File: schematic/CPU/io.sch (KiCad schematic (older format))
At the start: 28 parts, among them SW4 SW_DIP_x08, U72 74LS245, U73 74LS273, U74 ATmega328P-PU, U75 74LS374, U76 DC56-11EWA

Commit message: schematic finished
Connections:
- net labels added: d1a, d1b, d1c, d1d, d1e, d1f, d1g, out0, out1, out2, out3, out4, out5, out6, out7
- wire segments 104 -> 95
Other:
- moved on the sheet: R73, R74, R75, R76, R77, R78, R79, R80, R81, R82, R83, R84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

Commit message: schematic with henry
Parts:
- removed R73, R74, R75, R76, R77, R78, R79, R80, R81, R82, R83, R84, R85, R86, R87, R88, R89, R90, R91, R92, R93, R94: 1k, symbol Device:R
- removed SW4: SW_DIP_x08, symbol Switch:SW_DIP_x08
- removed U72: 74LS245, symbol 74xx:74LS245
- removed U74: ATmega328P-PU, Package_DIP:DIP-28_W7.62mm, symbol MCU_Microchip_ATmega:ATmega328P-PU
- removed U75: 74LS374, symbol 74xx:74LS374
- removed U76: DC56-11EWA, Display_7Segment:DA56-11SURKWA, symbol Display_Character:DC56-11EWA
- added RN10: 10k, Resistor_THT:R_Array_SIP9, symbol Device:R_Network08
- added SW10, SW11: SW_Coded_SH-7050, symbol Switch:SW_Coded_SH-7050
- added U88: 74F521, symbol 8bitCPU-rescue:74F521
- added U89, U90: 74LS32, symbol 74xx:74LS32
- added U91: 74LS245, symbol 74xx:74LS245
- added U93, U94: 5082_7340, symbol 8bitCPU-rescue:5082_7340
- renumbered U73 to U92
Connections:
- net labels added: ioAddr0, ioAddr1, ioAddr2, ioAddr3, ioAddr4, ioAddr5, ioAddr6, ioAddr7, ioSelect, ~ioOE~, ~ioWE~
- net labels removed: d1a, d1b, d1c, d1d, d1e, d1f, d1g, out0, out1, out2, out3, out4, out5, out6, out7, outWRPulse, sr0, sr1, sr2, sr3, sr4, sr5, sr6, ~inOE~
- wire segments 95 -> 113
- no-connect marks 8 -> 0
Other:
- note added: "Invertierung beachten!"
- moved on the sheet: U92

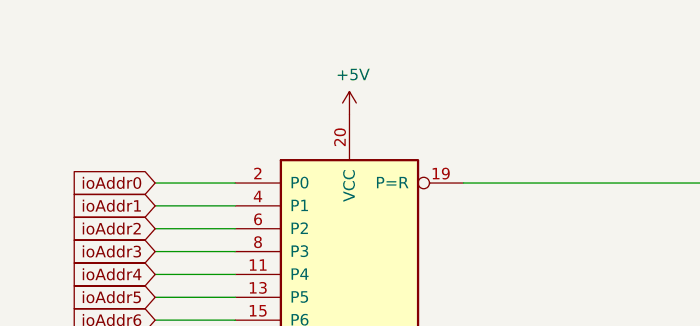
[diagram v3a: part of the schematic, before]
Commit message: updated verilog from schematic
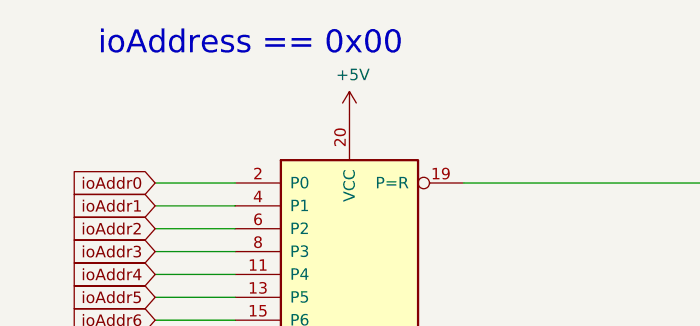
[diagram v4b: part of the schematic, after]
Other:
- note added: "ioAddress == 0x00"
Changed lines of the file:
@@
 Wire Wire Line
 	7000 2450 7550 2450
+Text Notes 1850 1250 0    100  ~ 0
+ioAddress == 0x00
 $EndSCHEMATC

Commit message: renamed project
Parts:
- U88: symbol 8bitCPU-rescue:74F521 -> MEDiC-rescue:74F521
- U93, U94: symbol 8bitCPU-rescue:5082_7340 -> MEDiC-rescue:5082_7340
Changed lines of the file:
@@
 	5700 2450 6000 2450
 $Comp
-L 8bitCPU-rescue:74F521 U88
+L MEDiC-rescue:74F521 U88
 U 1 1 62CAE1E1
 P 3550 2600
@@
 	5800 4350 5950 4350
 $Comp
-L 8bitCPU-rescue:5082_7340 U93
+L MEDiC-rescue:5082_7340 U93
 U 1 1 62D5B960
 P 8850 2250
@@
 	8100 3700 7550 3700
 $Comp
-L 8bitCPU-rescue:5082_7340 U94
+L MEDiC-rescue:5082_7340 U94
 U 1 1 62D6D0EE
 P 8850 3900

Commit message: renamed project
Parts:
- U88: symbol MEDiC-rescue:74F521 -> EDiC-rescue:74F521
- U93, U94: symbol MEDiC-rescue:5082_7340 -> EDiC-rescue:5082_7340
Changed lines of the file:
@@
 	5700 2450 6000 2450
 $Comp
-L MEDiC-rescue:74F521 U88
+L EDiC-rescue:74F521 U88
 U 1 1 62CAE1E1
 P 3550 2600
@@
 	5800 4350 5950 4350
 $Comp
-L MEDiC-rescue:5082_7340 U93
+L EDiC-rescue:5082_7340 U93
 U 1 1 62D5B960
 P 8850 2250
@@
 	8100 3700 7550 3700
 $Comp
-L MEDiC-rescue:5082_7340 U94
+L EDiC-rescue:5082_7340 U94
 U 1 1 62D6D0EE
 P 8850 3900

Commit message: restructured folders
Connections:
- net ioSelect renamed ~ioCE~
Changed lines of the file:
@@
 $EndComp
 Text GLabel 2000 3600 0    50   Input ~ 0
-ioSelect
+~ioCE~
 Text GLabel 2100 1800 0    50   Input ~ 0
 ioAddr0
@@
 Text Notes 1850 1250 0    100  ~ 0
 ioAddress == 0x00
+Wire Notes Line
+	1650 3700 2050 3700
+Wire Notes Line
+	2050 3700 2050 3500
+Wire Notes Line
+	2050 3500 1650 3500
+Wire Notes Line
+	1650 3500 1650 3700
 $EndSCHEMATC
